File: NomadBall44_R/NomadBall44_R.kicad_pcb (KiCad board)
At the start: 2 copper layers, 144.8 x 96.5 mm, 56 parts, among them SW1 SW_Push, SW10 SW_Push, SW11 SW_Push, SW12 SW_Push, SW13 SW_Push, SW14 SW_Push, SW15 SW_Push, SW16 SW_Push, SW17 SW_Push, SW18 SW_Push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

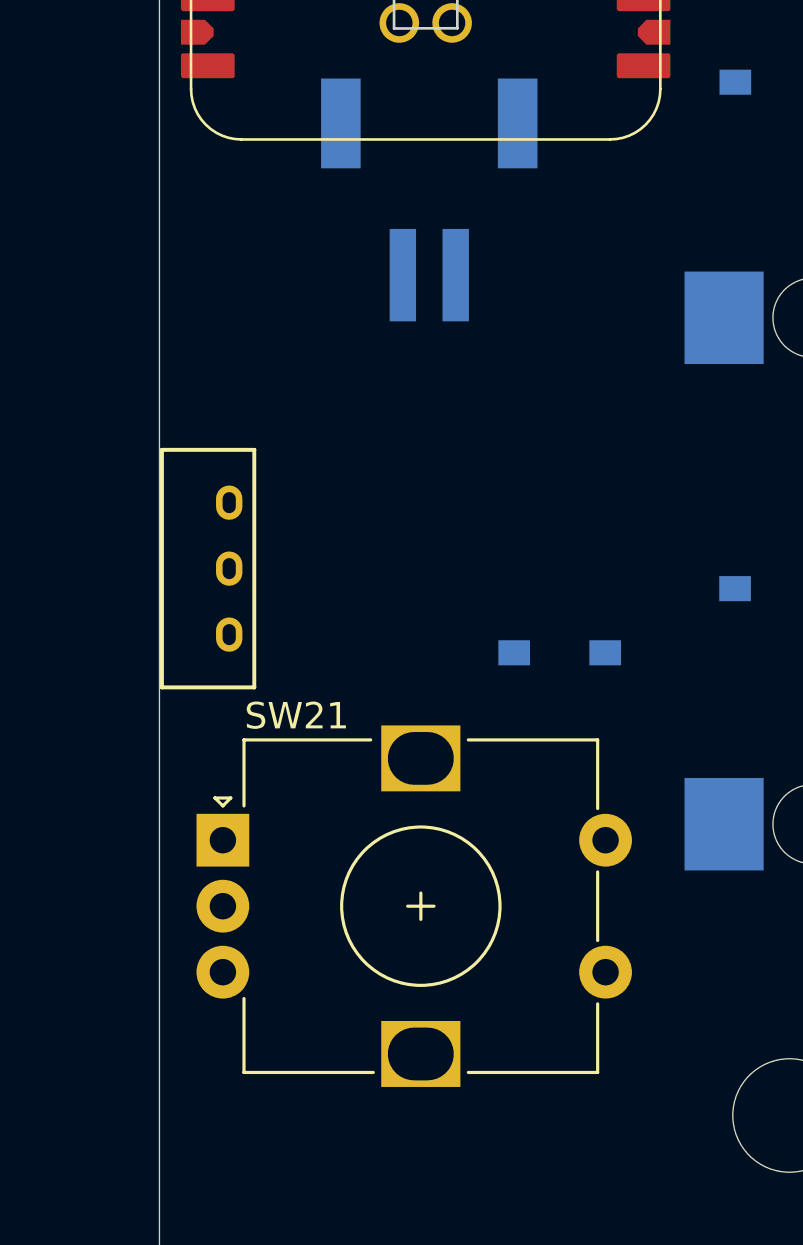
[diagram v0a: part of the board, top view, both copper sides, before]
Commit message: ロータリーエンコーダーの位置を微修正
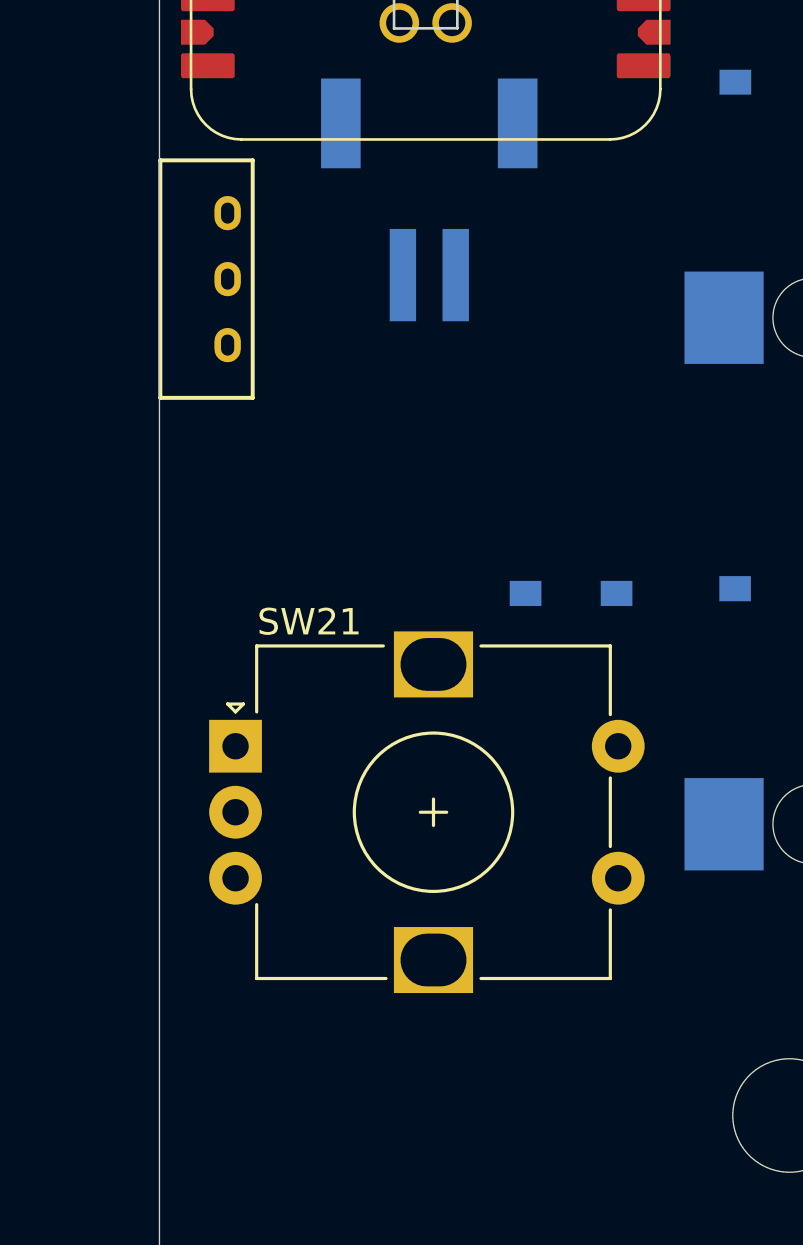
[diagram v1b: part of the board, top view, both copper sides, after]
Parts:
- moved SW23 11.0 mm to (87.0, 76.0)
- moved SW21 3.59 mm to (88.4, 93.7)
- moved D21 2.29 mm to (98.3, 87.9)
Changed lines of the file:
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@@
 	(footprint "NomadBall44:TGSW_MSK-12D19"
 		(layer "F.Cu")
-		(at 87.1 86.99 90)
+		(at 87.04 76.02 90)
 		(property "Reference" "SW23"
 			(at 0 -2 90)
@@
 	(footprint "NomadBall44:Diode_SMD"
 		(layer "F.Cu")
-		(at 97.893438 90.18)
+		(at 98.323438 87.93)
 		(descr "https://github.com/e3w2q/su120-keyboard (diode_SMD_rev2)")
 		(property "Reference" "D21"
@@
 	(footprint "Rotary_Encoder:RotaryEncoder_Alps_EC12E-Switch_Vertical_H20mm"
 		(layer "F.Cu")
-		(at 87.91 97.28)
+		(at 88.39 93.72)
 		(descr "Alps rotary encoder, EC12E... with switch, vertical shaft, http://www.alps.com/prod/info/E/HTML/Encoder/Incremental/EC12E/EC12E1240405.html & http://cdn-reichelt.de/documents/datenblatt/F100/402097STEC12E08.PDF")
 		(tags "rotary encoder")

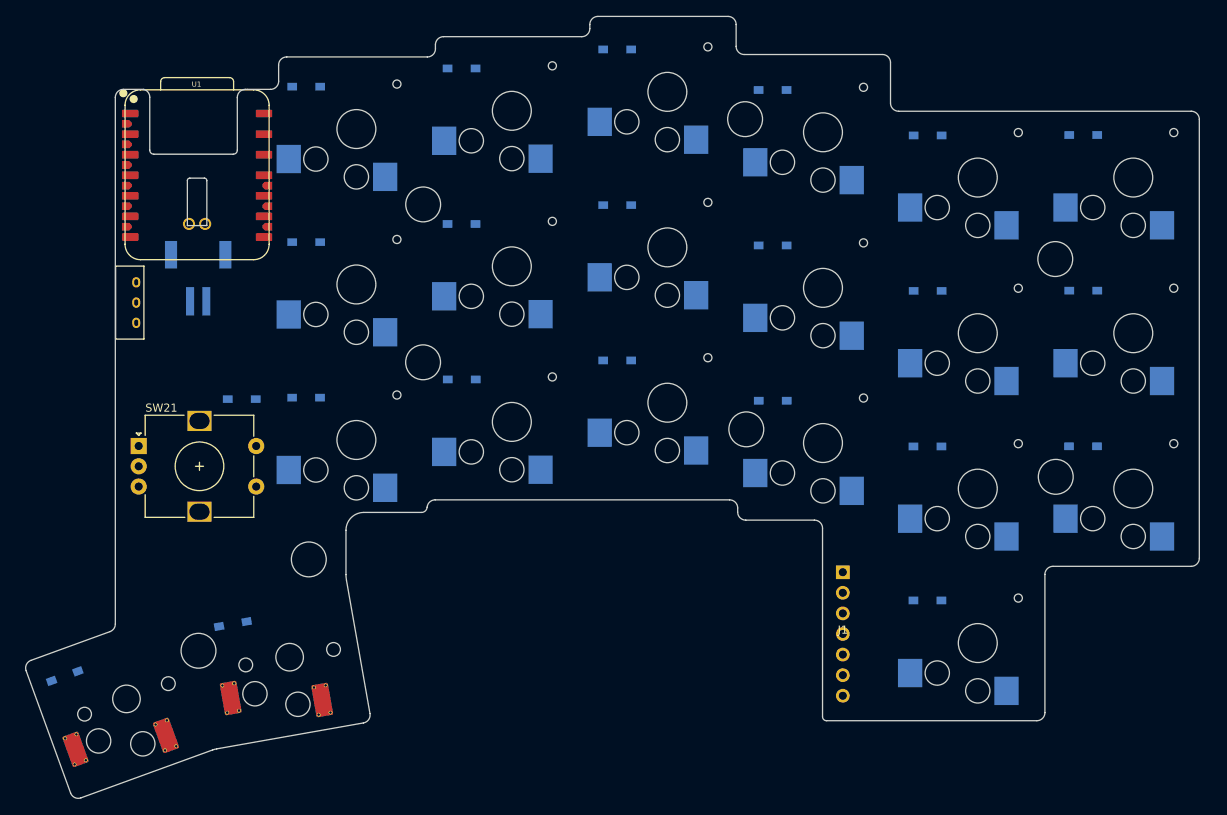
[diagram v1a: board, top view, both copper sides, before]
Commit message: PCB基盤の外形線を修正
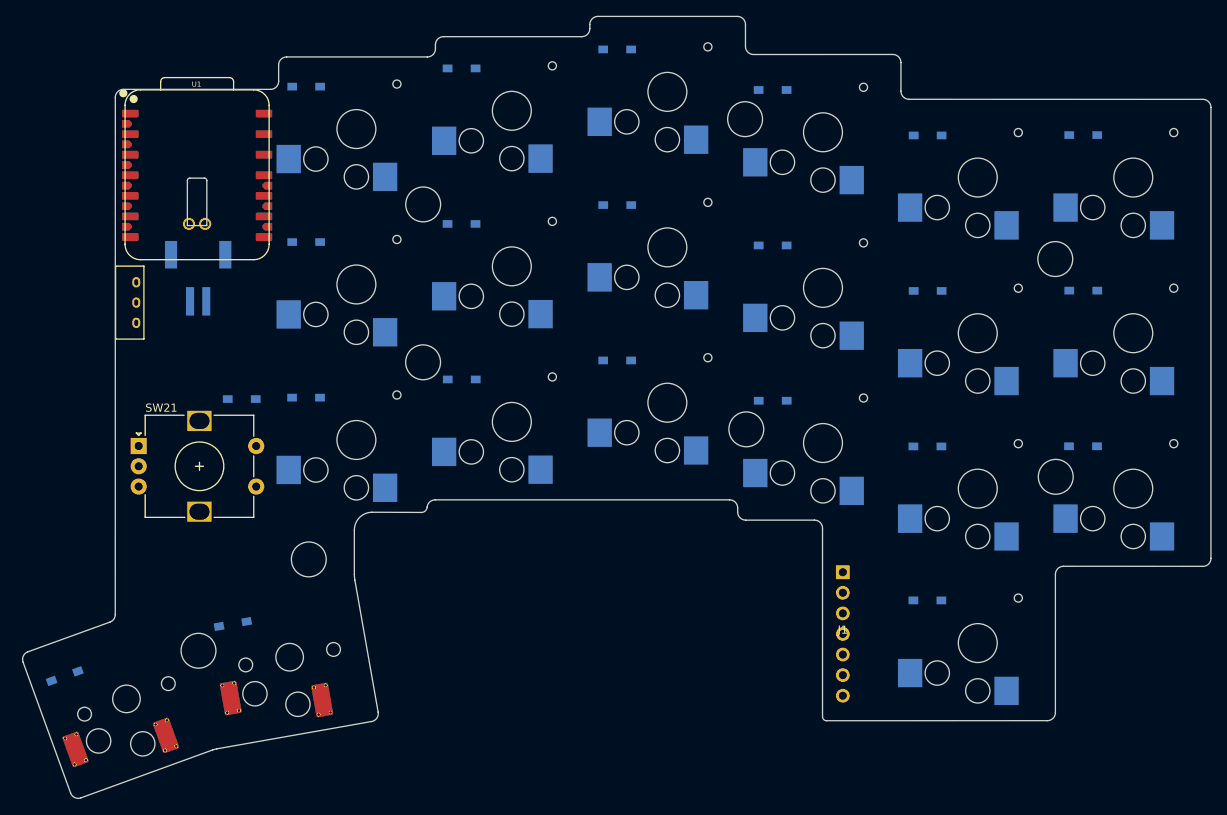
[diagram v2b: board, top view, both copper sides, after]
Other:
- board size 144.8 x 96.5 mm -> 146.6 x 96.5 mm

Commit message: トラックボール用の配線を追加 & 端面スルーホール向けに導体から基板端のクリアランスを0に設定
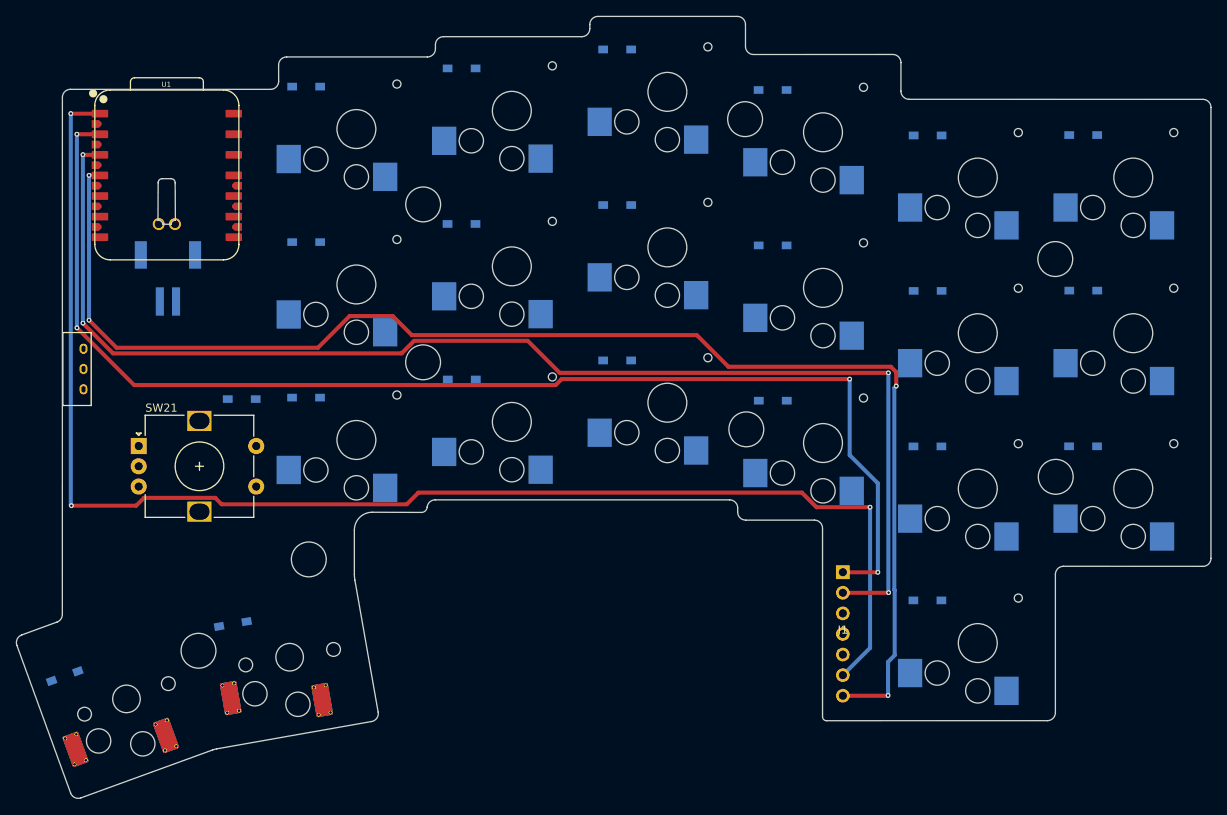
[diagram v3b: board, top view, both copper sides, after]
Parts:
- moved SW23 10.5 mm to (80.5, 84.2)
- moved BT1 3.73 mm to (92.0, 75.9)
- moved U1 3.73 mm to (91.9, 60.3)
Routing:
- net SDIO: track 0.00 -> 174.7 mm, vias 0 -> 3
- net MOTION: track 0.00 -> 170.7 mm, vias 0 -> 4
- net CS: track 0.00 -> 158.9 mm, vias 0 -> 4
- net SCLK: track 0.00 -> 154.9 mm, vias 0 -> 4
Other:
- board size 146.6 x 96.5 mm -> 147.4 x 96.5 mm

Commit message: トラックボールとバッテリー周りを配線
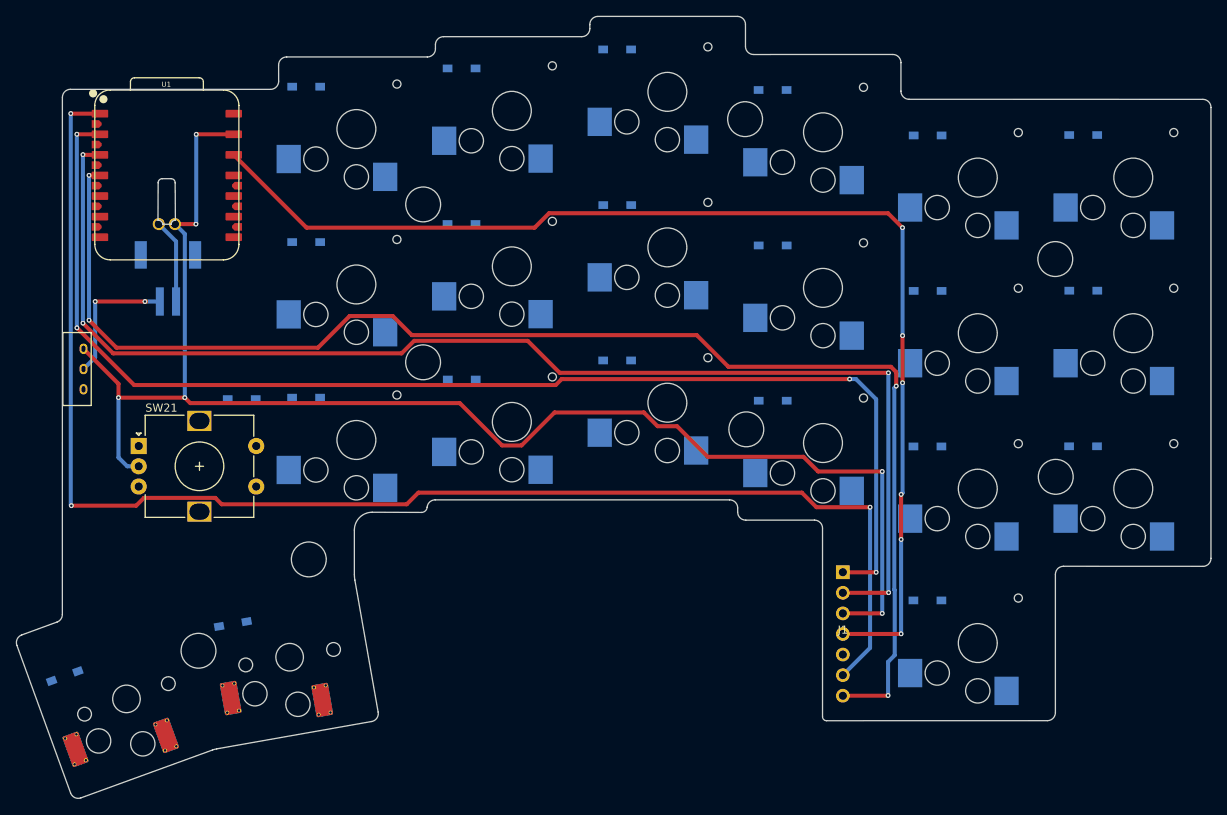
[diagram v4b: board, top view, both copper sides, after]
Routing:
- net GND: track 0.00 -> 182.4 mm, vias 0 -> 6
- net 3.3V: track 0.00 -> 145.1 mm, vias 0 -> 6
- net Net-(BT1--): track 0.00 -> 17.2 mm, vias 0 -> 2
- net Bat: track 0.00 -> 11.4 mm

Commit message: マイコンまわりの配線が完了 & ラベルの間違えを修正
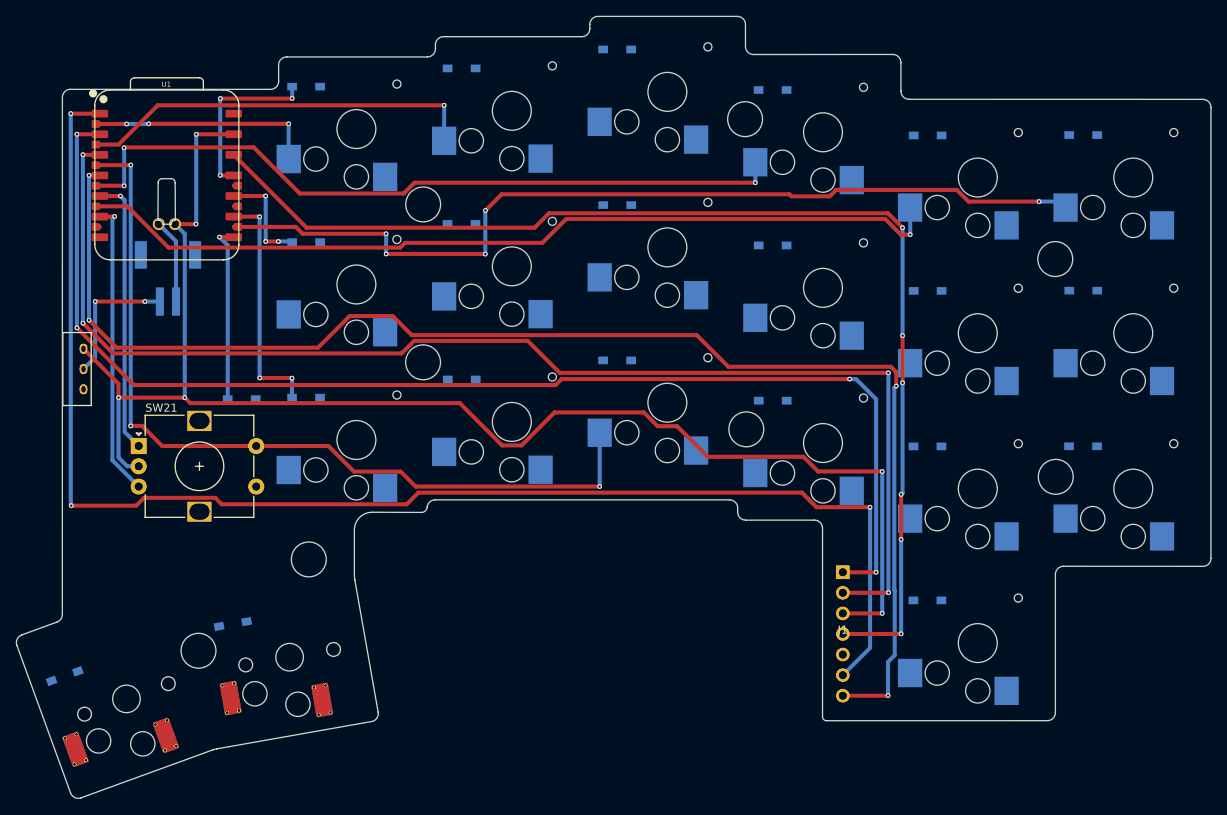
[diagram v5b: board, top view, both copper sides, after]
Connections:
- U1 pad 8: Row2 -> Row3
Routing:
- net Col5: track 0.00 -> 112.6 mm, vias 0 -> 5
- net Col4: track 0.00 -> 108.1 mm, vias 0 -> 1
- net Col2: track 0.00 -> 104.0 mm, vias 0 -> 3
- net Col3: track 0.00 -> 91.5 mm, vias 0 -> 3
- net Col1: track 0.00 -> 49.3 mm, vias 0 -> 1
- net RE_B: track 0.00 -> 36.6 mm, vias 0 -> 1
- net RE_A: track 0.00 -> 34.3 mm, vias 0 -> 1
- net Row2: track 0.00 -> 29.5 mm, vias 0 -> 3
- net Col0: track 0.00 -> 28.0 mm, vias 0 -> 3
- net Row3: track 0.00 -> 22.2 mm, vias 0 -> 1
- net Row0: track 0.00 -> 21.5 mm, vias 0 -> 3
- net Row1: track 0.00 -> 12.9 mm, vias 0 -> 3

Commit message: キースイッチまわりの配線完了
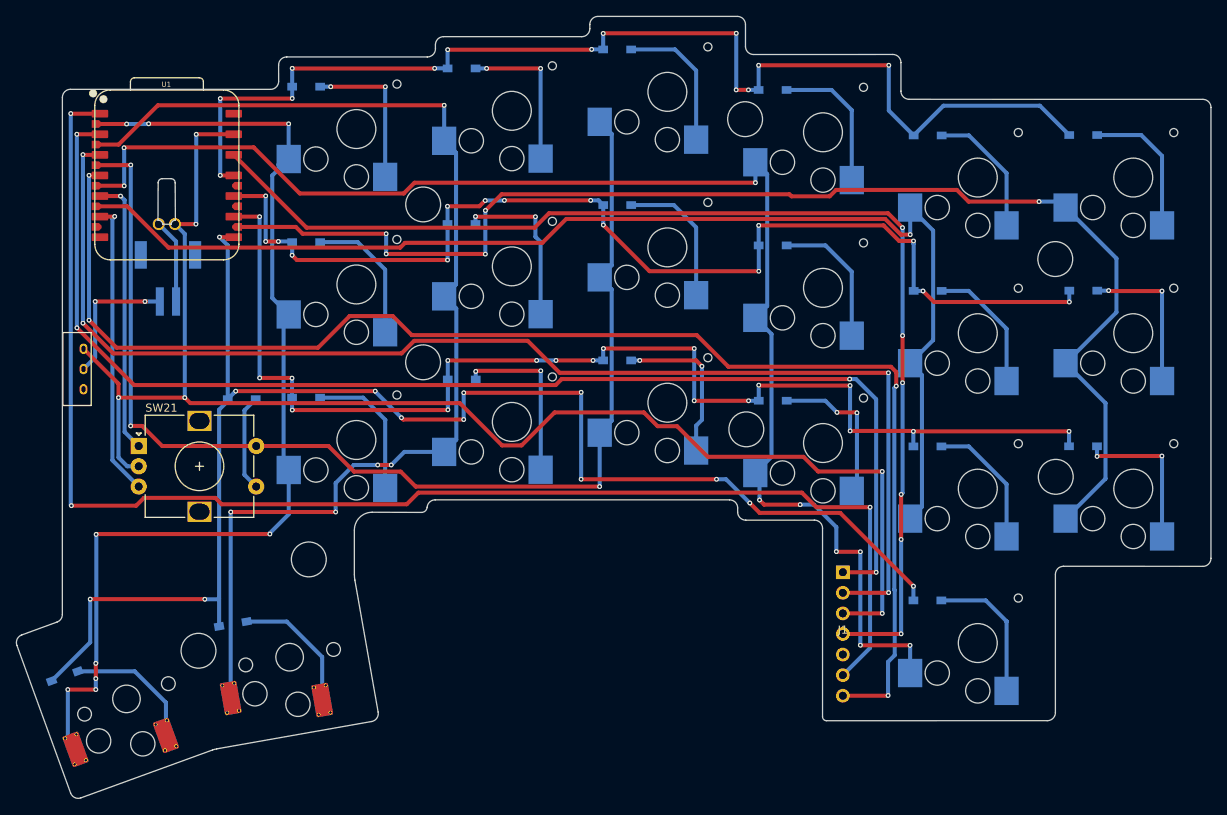
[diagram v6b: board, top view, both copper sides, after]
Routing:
- net Row3: track 22.2 -> 186.4 mm, vias 1 -> 13
- net Row1: track 12.9 -> 137.2 mm, vias 3 -> 15
- net Row2: track 29.5 -> 152.2 mm, vias 3 -> 18
- net Row0: track 21.5 -> 143.9 mm, vias 3 -> 13
- net Col0: track 28.0 -> 130.9 mm, vias 3 -> 9
- net Col1: track 49.3 -> 144.5 mm, vias 1 -> 5
- net Col3: track 91.5 -> 174.5 mm, vias 3 -> 9
- net Col5: track 112.6 -> 160.3 mm
- net Col4: track 108.1 -> 150.0 mm
- net Col2: track 104.0 -> 144.8 mm
- net Net-(D14-A): track 0.00 -> 21.3 mm, vias 0 -> 2
- net Net-(D8-A): track 0.00 -> 20.6 mm, vias 0 -> 2
- net Net-(D15-A): track 0.00 -> 19.7 mm, vias 0 -> 2
- net Net-(D18-A): track 0.00 -> 19.2 mm, vias 0 -> 2
- net Net-(D16-A): track 0.00 -> 19.2 mm, vias 0 -> 2
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
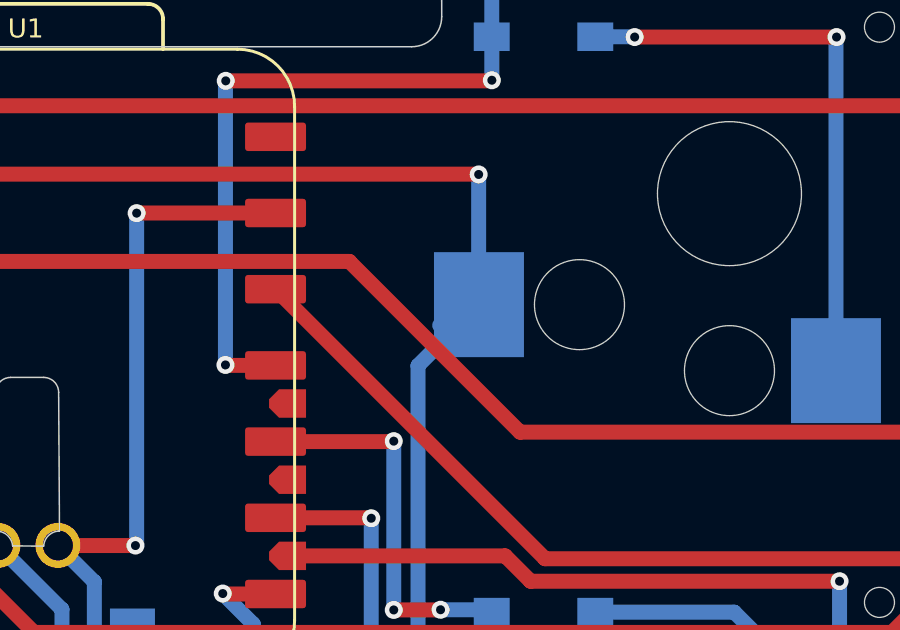
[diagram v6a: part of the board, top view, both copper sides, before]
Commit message: トッププレートに不要なエリアを削除
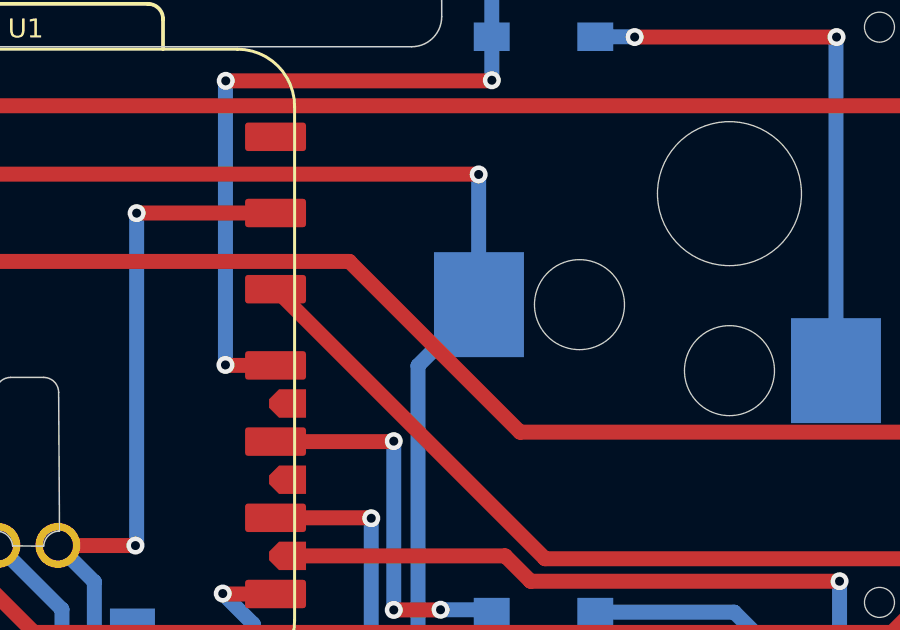
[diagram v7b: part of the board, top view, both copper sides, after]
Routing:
- net Col0: track 130.9 -> 130.0 mm
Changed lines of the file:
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@@
-	)
-	(segment
-		(start 106.28 58.31)
-		(end 105.59 59)
-		(width 0.5)
-		(layer "B.Cu")
-		(net 36)
 	)
 	(segment
